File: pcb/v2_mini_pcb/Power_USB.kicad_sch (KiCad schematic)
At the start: 34 parts, among them J6 USB4105-GF-A, U10 TPS63802DLAR, U6 TPD4EUSB30, U8 BQ25622RYKR, U9 MAX17048G_T10

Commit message: not sure
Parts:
- added R27: 10k, symbol Device:R_Small_US
- C18: value 47nF -> 4.7uF
- R14: value 5.62k -> 5.23k
- TH1: value 10k -> 103KT1608T-1P
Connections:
- net +3V3: now also R27.2
- net at C17.1: now also U8.1 (BTST); no longer U8.3 (PG)
- new net CHG_PG: R27.1, U8.3 (PG)
- no-connect marks 9 -> 8
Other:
- moved on the sheet: U8

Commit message: add mpn and footprints for some
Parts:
- added C25, C26: DNP, Capacitor_SMD:C_01005_0402Metric, symbol Device:C_Small
- added R28: 75k, symbol Device:R_Small_US
- added R29: 100k, symbol Device:R_Small_US
- C16: footprint (none) -> Capacitor_SMD:C_0201_0603Metric; MPN (none) -> CL05A105KA5NQNC
- C17: footprint (none) -> Capacitor_SMD:C_0201_0603Metric; MPN (none) -> CL10B473KB8NNNC
- C18: footprint (none) -> Capacitor_SMD:C_01005_0402Metric; MPN (none) -> CL05A475MP5NRNC
- C19, C21: footprint (none) -> Capacitor_SMD:C_01005_0402Metric; MPN (none) -> CL05B104KB54PNC
- C20, C33: footprint (none) -> Capacitor_SMD:C_0201_0603Metric; MPN (none) -> CL10A106KP8NNNC
- C30, C31, C32: footprint (none) -> Capacitor_SMD:C_0805_2012Metric; MPN (none) -> CL21A226MAQNNNE
- C34: footprint (none) -> Capacitor_SMD:C_0201_0603Metric; MPN (none) -> CL10A226MQ8NRNC
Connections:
- net GND: now also C25.2, C26.2, R29.1
- net USB_DN: now also C25.1
- net USB_DP: now also C26.1
- net at C16.2, J6.A4_B9 (VBUS), J6.B4_A9 (VBUS__1)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: now also R28.2
- new net USB_VBUS_S: R28.1, R29.2

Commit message: finish off mpn and footprints
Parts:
- C16: footprint Capacitor_SMD:C_0201_0603Metric -> Capacitor_SMD:C_0603_1608Metric; MPN CL05A105KA5NQNC -> GMK107AB7105KAHT
- C17: footprint Capacitor_SMD:C_0201_0603Metric -> Capacitor_SMD:C_0402_1005Metric; MPN CL10B473KB8NNNC -> GRM155R71E473KA88D
- C18: footprint Capacitor_SMD:C_01005_0402Metric -> Capacitor_SMD:C_0603_1608Metric; MPN CL05A475MP5NRNC -> GRM188R61E475KE11D
- C19: footprint Capacitor_SMD:C_01005_0402Metric -> Capacitor_SMD:C_0402_1005Metric; MPN CL05B104KB54PNC -> GRM155R71H104KE14D
- C20: footprint Capacitor_SMD:C_0201_0603Metric -> Capacitor_SMD:C_0805_2012Metric; MPN CL10A106KP8NNNC -> C2012X5R1E106K125AB
- C21: footprint Capacitor_SMD:C_01005_0402Metric -> Capacitor_SMD:C_0402_1005Metric; MPN CL05B104KB54PNC -> GRM155R71C104KA88D
- C25, C26: footprint Capacitor_SMD:C_01005_0402Metric -> Capacitor_SMD:C_0402_1005Metric; MPN CL05A105KA5NQNC -> DNP
- C30, C31, C32: MPN CL21A226MAQNNNE -> GRM21BR61A226ME44L
- C33: footprint Capacitor_SMD:C_0201_0603Metric -> Capacitor_SMD:C_0603_1608Metric; MPN CL10A106KP8NNNC -> GRM188R61A106ME69D
- C34: footprint Capacitor_SMD:C_0201_0603Metric -> Capacitor_SMD:C_0603_1608Metric; MPN CL10A226MQ8NRNC -> GRM188R61A226ME15D
- FB1, FB2: footprint (none) -> Inductor_SMD:L_0805_2012Metric; MPN (none) -> MPZ2012S601ATD25
- J6: footprint USB4105-GF-A:GCT_USB4105-GF-A -> all:GCT_USB4105-GF-A; MPN (none) -> USB4105-GF-A
- L4: footprint (none) -> Inductor_SMD:L_1008_2520Metric; MPN (none) -> DFE252012F-1R0M=P2
- L5: footprint (none) -> Inductor_SMD:L_Murata_DFE201610P; MPN (none) -> DFE201612E-R47M=P2
- R11, R12, R16, R21: footprint (none) -> Resistor_SMD:R_0402_1005Metric; MPN (none) -> 0402WGF5101TCE
- R13: footprint (none) -> Resistor_SMD:R_0402_1005Metric; MPN (none) -> RC0402FR-075K62L
- R14: footprint (none) -> Resistor_SMD:R_0402_1005Metric; MPN (none) -> RC0402FR-075K23L
- R15: footprint (none) -> Resistor_SMD:R_0402_1005Metric; MPN (none) -> CRCW040230K1FKED
- R22, R23, R27, R3: footprint (none) -> Resistor_SMD:R_0402_1005Metric; MPN (none) -> 0402WGF1002TCE
- R25: footprint (none) -> Resistor_SMD:R_0603_1608Metric; MPN (none) -> RC0603FR-07511KL
- R26: footprint (none) -> Resistor_SMD:R_0603_1608Metric; MPN (none) -> RC0603FR-0791KL
- R28: footprint (none) -> Resistor_SMD:R_0402_1005Metric; MPN (none) -> 0402WGF7502TCE
- R29: footprint (none) -> Resistor_SMD:R_0402_1005Metric; MPN (none) -> 0402WGF1003TCE
- TH1: footprint (none) -> Resistor_SMD:R_0603_1608Metric; MPN (none) -> NCU18XH103F60RB
- U10: footprint TPS63802DLAR:VREG_TPS63802DLAR -> all:VREG_TPS63802DLAR; MPN (none) -> TPS63802DLAR
- U6: MPN (none) -> TPD4EUSB30DQAR
- U8: value BQ25622RYKR -> BQ25622ERYKR; footprint WQFN-HR18__RYK_TEX -> all:WQFN-HR18__RYK_TEX; symbol all:BQ25622RYKR -> all:BQ25622ERYKR; MPN (none) -> BQ25622ERYKR
- U9: footprint MAX17048G_T10:SON50P200X200X80-9N -> all:SON50P200X200X80-9N; MPN (none) -> MAX17048G+T10

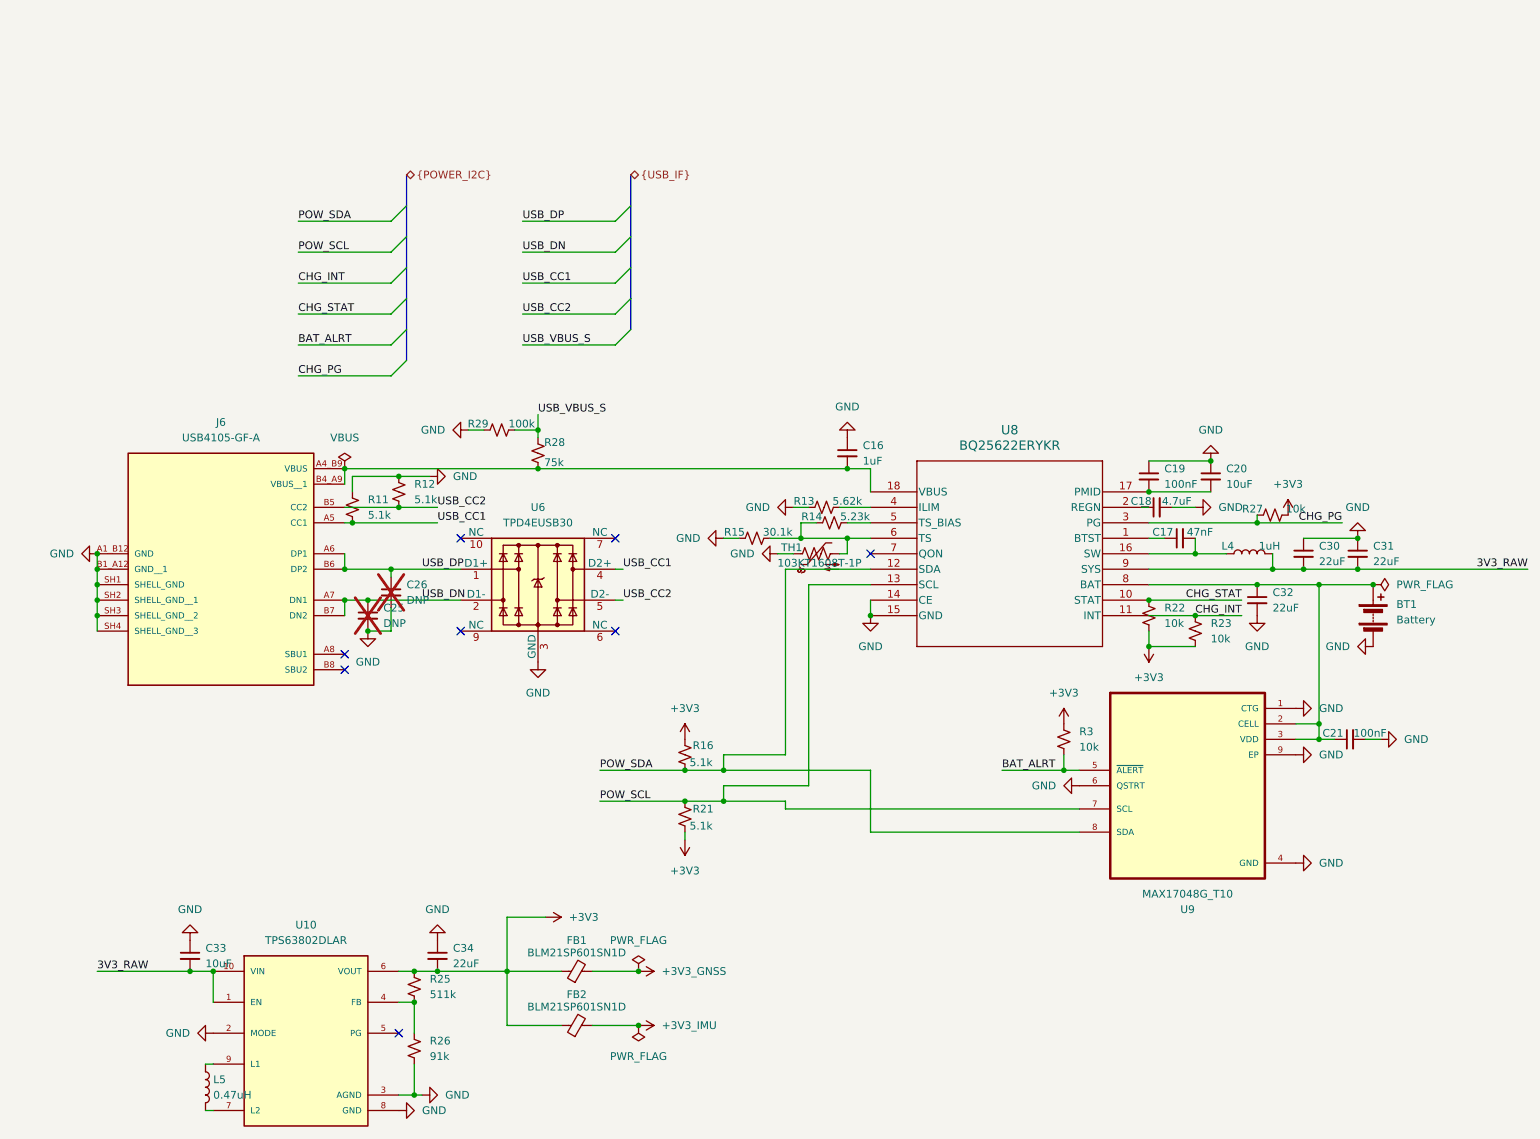
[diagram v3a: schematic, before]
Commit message: finish footprint matching
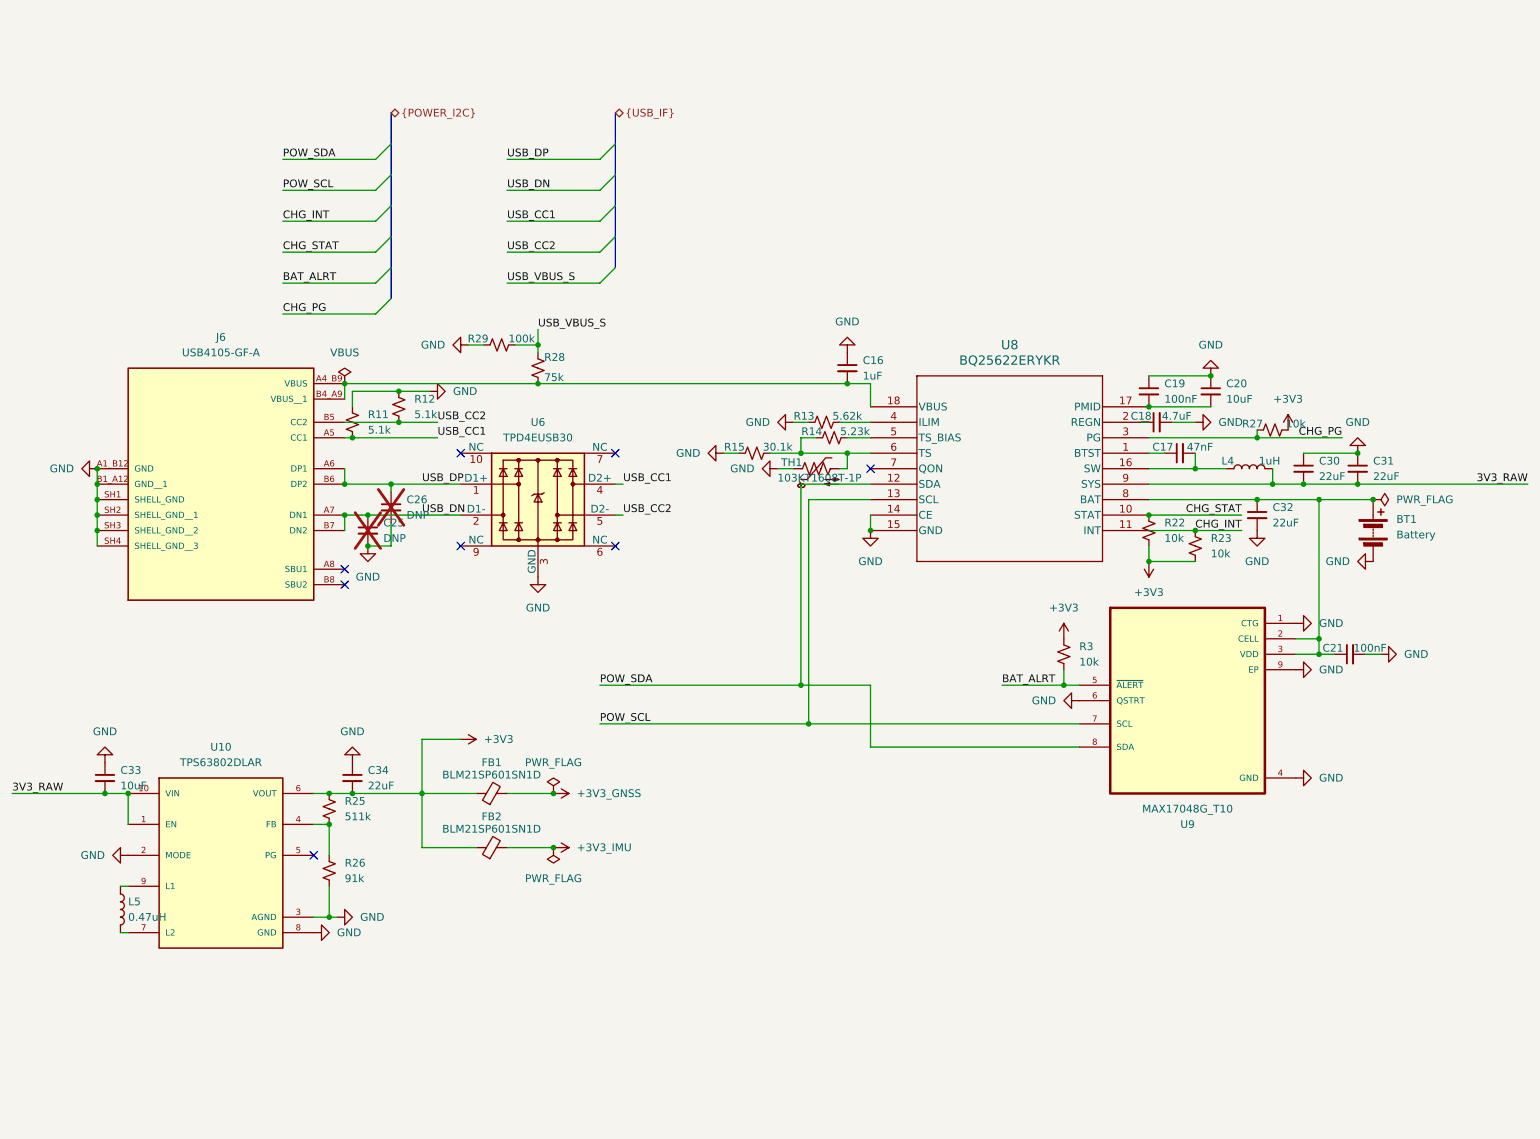
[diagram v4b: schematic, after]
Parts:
- removed R16, R21: 5.1k, Resistor_SMD:R_0402_1005Metric, symbol Device:R_Small_US
- C16: Dielectric (none) -> X7R; DigiKey_PN (none) -> 587-3352-1-ND; Manufacturer (none) -> Taiyo Yuden; Supplier (none) -> DigiKey; Tolerance (none) -> 10%; Voltage (none) -> 35V
- C17: Dielectric (none) -> X7R; DigiKey_PN (none) -> 490-3254-1-ND; Manufacturer (none) -> Murata Electronics; Supplier (none) -> DigiKey; Tolerance (none) -> 10%; Voltage (none) -> 25V
- C18: Dielectric (none) -> X5R; DigiKey_PN (none) -> 490-7203-1-ND; Manufacturer (none) -> Murata Electronics; Supplier (none) -> DigiKey; Tolerance (none) -> 10%; Voltage (none) -> 25V
- C19: Dielectric (none) -> X7R; JLCPCB_PN (none) -> C307331; LCSC (none) -> C307331; MPN GRM155R71H104KE14D -> CL05B104KB54PNC; Manufacturer (none) -> Samsung Electro-Mechanics; Supplier (none) -> JLCPCB Basic; Tolerance (none) -> 10%; Voltage (none) -> 50V
- C20: Dielectric (none) -> X5R; JLCPCB_PN (none) -> C15850; LCSC (none) -> C15850; MPN C2012X5R1E106K125AB -> CL21A106KAYNNNE; Manufacturer (none) -> Samsung Electro-Mechanics; Supplier (none) -> JLCPCB Basic; Tolerance (none) -> 10%; Voltage (none) -> 25V
- C21: Dielectric (none) -> X7R; JLCPCB_PN (none) -> C1525; LCSC (none) -> C1525; MPN GRM155R71C104KA88D -> CL05B104KO5NNNC; Manufacturer (none) -> Samsung Electro-Mechanics; Supplier (none) -> JLCPCB Basic; Tolerance (none) -> 10%; Voltage (none) -> 16V
- C30, C31, C32: Dielectric (none) -> X5R; JLCPCB_PN (none) -> C45783; LCSC (none) -> C45783; MPN GRM21BR61A226ME44L -> CL21A226MAQNNNE; Manufacturer (none) -> Samsung Electro-Mechanics; Supplier (none) -> JLCPCB Basic; Tolerance (none) -> 20%; Voltage (none) -> 25V
- C33: Dielectric (none) -> X5R; JLCPCB_PN (none) -> C19702; LCSC (none) -> C19702; MPN GRM188R61A106ME69D -> CL10A106KP8NNNC; Manufacturer (none) -> Samsung Electro-Mechanics; Supplier (none) -> JLCPCB Basic; Tolerance (none) -> 10%; Voltage (none) -> 10V
- C34: Dielectric (none) -> X5R; DigiKey_PN (none) -> 490-GRT188R61A226ME13DCT-ND; MPN GRM188R61A226ME15D -> GRT188R61A226ME13D; Manufacturer (none) -> Murata Electronics; Supplier (none) -> DigiKey; Tolerance (none) -> 20%; Voltage (none) -> 10V
- J6: MANUFACTURER GCT -> (none); Manufacturer (none) -> GCT
- U10: MANUFACTURER Texas Instruments -> (none); Manufacturer (none) -> Texas Instruments
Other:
- moved on the sheet: BT1, C16, C17, C18, C19, C20, C21, C25, C26, C30, C31, C32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

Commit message: vbus connection
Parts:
- added R32, R33: 22k, Resistor_SMD:R_0402_1005Metric, symbol Device:R_Small_US
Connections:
- net USB_CC1: now also U6.7 (NC), R33.1, R33.2
- net USB_CC2: now also U6.6 (NC), R32.1, R32.2
- net USB_DN: now also U6.9 (NC)
- net USB_DP: now also U6.10 (NC)
- no-connect marks 8 -> 4
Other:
- moved on the sheet: R12

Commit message: fix last erc errors
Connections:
- net USB_CC1: no longer J6.A5 (CC1), R11.2, R33.1, U6.4 (D2+), U6.7 (NC)
- net USB_CC2: no longer J6.B5 (CC2), R12.2, R32.1, U6.5 (D2-), U6.6 (NC)
- new net USB_CC1_pre: J6.A5 (CC1), R11.2, R33.1, U6.4 (D2+), U6.7 (NC)
- new net USB_CC2_pre: J6.B5 (CC2), R12.2, R32.1, U6.5 (D2-), U6.6 (NC)
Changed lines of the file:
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@@
+	)
+	(junction
+		(at 82.55 67.31)
+		(diameter 0)
+		(color 0 0 0 0)
 	)
 	(junction
@@
 	(junction
 		(at 38.1 128.27)
+		(diameter 0)
+		(color 0 0 0 0)
+	)
+	(junction
+		(at 82.55 69.85)
 		(diameter 0)
 		(color 0 0 0 0)
@@
 	(wire
 		(pts
+			(xy 82.55 72.39) (xy 82.55 69.85)
+		)
+		(stroke
+			(width 0)
+			(type default)
+		)
+	)
+	(wire
+		(pts
 			(xy 115.57 116.84) (xy 149.86 116.84)
 		)
@@
 	(wire
 		(pts
-			(xy 80.01 67.31) (xy 86.36 67.31)
+			(xy 80.01 67.31) (xy 82.55 67.31)
 		)
 		(stroke
@@
 	(wire
 		(pts
-			(xy 74.93 69.85) (xy 86.36 69.85)
+			(xy 74.93 69.85) (xy 82.55 69.85)
 		)
 		(stroke
@@
 		)
 	)
-	(wire
-		(pts
-			(xy 119.38 82.55) (xy 118.11 82.55)
-		)
-		(stroke
-			(width 0)
-			(type default)
-		)
-	)
 	(bus
 		(pts
@@
 	(wire
 		(pts
+			(xy 82.55 67.31) (xy 86.36 67.31)
+		)
+		(stroke
+			(width 0)
+			(type default)
+		)
+	)
+	(wire
+		(pts
 			(xy 149.86 80.01) (xy 149.86 116.84)
 		)
@@
 	(wire
 		(pts
+			(xy 82.55 69.85) (xy 86.36 69.85)
+		)
+		(stroke
+			(width 0)
+			(type default)
+		)
+	)
+	(wire
+		(pts
 			(xy 33.02 82.55) (xy 33.02 85.09)
 		)
@@
 	(wire
 		(pts
+			(xy 82.55 66.04) (xy 82.55 67.31)
+		)
+		(stroke
+			(width 0)
+			(type default)
+		)
+	)
+	(wire
+		(pts
 			(xy 154.94 74.93) (xy 156.21 74.93)
 		)
@@
 		)
 	)
-	(wire
-		(pts
-			(xy 119.38 77.47) (xy 118.11 77.47)
-		)
-		(stroke
-			(width 0)
-			(type default)
-		)
-	)
 	(bus
 		(pts
@@
 			(width 0)
 			(type default)
+		)
+	)
+	(label "USB_CC1_pre"
+		(at 82.55 72.39 0)
+		(effects
+			(font
+				(size 1.27 1.27)
+			)
+			(justify left bottom)
+		)
+	)
+	(label "USB_CC2_pre"
+		(at 118.11 82.55 0)
+		(effects
+			(font
+				(size 1.27 1.27)
+			)
+			(justify left bottom)
 		)
 	)
@@
 		)
 	)
-	(label "USB_CC2"
-		(at 119.38 82.55 0)
+	(label "USB_CC2_pre"
+		(at 82.55 66.04 0)
 		(effects
 			(font
@@
 		)
 	)
-	(label "USB_CC1"
-		(at 119.38 77.47 0)
-		(effects
-			(font
-				(size 1.27 1.27)
-			)
-			(justify left bottom)
-		)
-	)
 	(label "USB_DN"
 		(at 100.33 29.21 0)
@@
 		)
 	)
+	(label "USB_CC1_pre"
+		(at 118.11 77.47 0)
+		(effects
+			(font
+				(size 1.27 1.27)
+			)
+			(justify left bottom)
+		)
+	)
 	(label "USB_DP"
 		(at 100.33 24.13 0)
@@
 		(effects
 			(font
-				(size 1.27 1.27)
-			)
-			(justify left bottom)
-		)
-	)
-	(label "USB_CC1"
-		(at 81.28 69.85 0)
-		(effects
-			(font
-				(size 1.27 1.27)
-			)
-			(justify left bottom)
-		)
-	)
-	(label "USB_CC2"
-		(at 85.09 67.31 0)
-		(effects
-			(font

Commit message: fix drc problems nad d+d- and sd
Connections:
- net USB_DN: now also C26.1, J6.A6 (DP1), J6.B6 (DP2), U6.1 (D1+), U6.10 (NC); no longer C25.1, J6.A7 (DN1), J6.B7 (DN2), U6.2 (D1-), U6.9 (NC)
- net USB_DP: now also C25.1, J6.A7 (DN1), J6.B7 (DN2), U6.2 (D1-), U6.9 (NC); no longer C26.1, J6.A6 (DP1), J6.B6 (DP2), U6.1 (D1+), U6.10 (NC)
